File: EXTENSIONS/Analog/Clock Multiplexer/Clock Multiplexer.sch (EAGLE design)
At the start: 13 parts

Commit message: update clock multiplexer
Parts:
- removed SJ1: (no value), microbuilder:SOLDERJUMPERREFLOW
- added AUTOMATED_CLOCK_ON_OFF: (no value), adafruit:EG1218S
- renumbered R_MANUAL_CLOCK_PULL_DOWN to R_MANUAL_CLOCK_PULL_DOWN_1K
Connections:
- net N$2: now also AUTOMATED_CLOCK_ON_OFF.P; no longer SJ1.2
- net TMR555_OUTPUT_2: now also AUTOMATED_CLOCK_ON_OFF.O; no longer SJ1.1
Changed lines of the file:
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@@
 <part name="GND8" library="supply1" deviceset="GND" device=""/>
 <part name="MANUAL_CLOCK" library="switch-omron" deviceset="10-XX" device=""/>
-<part name="R_MANUAL_CLOCK_PULL_DOWN" library="adafruit" deviceset="R-US_" device="R1206"/>
+<part name="R_MANUAL_CLOCK_PULL_DOWN_1K" library="adafruit" deviceset="R-US_" device="R1206"/>
 <part name="GND9" library="supply1" deviceset="GND" device=""/>
-<part name="SJ1" library="microbuilder" deviceset="SOLDERJUMPER" device="REFLOW"/>
 <part name="DIODE_1N5817" library="diode" deviceset="1N821" device=""/>
+<part name="AUTOMATED_CLOCK_ON_OFF" library="adafruit" deviceset="EG1218" device="S"/>
 </parts>
 <sheets>
@@
 <instance part="GND8" gate="1" x="-66.04" y="81.28"/>
 <instance part="MANUAL_CLOCK" gate="1" x="-73.66" y="53.34"/>
-<instance part="R_MANUAL_CLOCK_PULL_DOWN" gate="G$1" x="-86.36" y="40.64"/>
+<instance part="R_MANUAL_CLOCK_PULL_DOWN_1K" gate="G$1" x="-86.36" y="40.64"/>
 <instance part="GND9" gate="1" x="-106.68" y="40.64" rot="R270"/>
-<instance part="SJ1" gate="1" x="-40.64" y="129.54"/>
 <instance part="DIODE_1N5817" gate="1" x="-25.4" y="129.54" rot="R180"/>
+<instance part="AUTOMATED_CLOCK_ON_OFF" gate="1" x="-48.26" y="127" smashed="yes" rot="R90">
+<attribute name="NAME" x="-43.053" y="136.652" size="1.778" layer="95" rot="R180"/>
+<attribute name="VALUE" x="-51.435" y="123.19" size="1.778" layer="96" rot="R180"/>
+</instance>
 </instances>
 <busses>
@@
 <segment>
 <pinref part="GND9" gate="1" pin="GND"/>
-<pinref part="R_MANUAL_CLOCK_PULL_DOWN" gate="G$1" pin="1"/>
+<pinref part="R_MANUAL_CLOCK_PULL_DOWN_1K" gate="G$1" pin="1"/>
 <wire x1="-104.14" y1="40.64" x2="-91.44" y2="40.64" width="0.1524" layer="91"/>
 </segment>
@@
 <wire x1="-71.12" y1="48.26" x2="-71.12" y2="40.64" width="0.1524" layer="91"/>
 <label x="-71.12" y="38.1" size="1.778" layer="95"/>
-<pinref part="R_MANUAL_CLOCK_PULL_DOWN" gate="G$1" pin="2"/>
+<pinref part="R_MANUAL_CLOCK_PULL_DOWN_1K" gate="G$1" pin="2"/>
 <wire x1="-71.12" y1="40.64" x2="-71.12" y2="35.56" width="0.1524" layer="91"/>
 <wire x1="-81.28" y1="40.64" x2="-71.12" y2="40.64" width="0.1524" layer="91"/>
@@
 </segment>
 <segment>
-<pinref part="SJ1" gate="1" pin="1"/>
-<wire x1="-45.72" y1="129.54" x2="-60.96" y2="129.54" width="0.1524" layer="91"/>
-<label x="-60.96" y="129.54" size="1.778" layer="95" rot="R180"/>
+<pinref part="AUTOMATED_CLOCK_ON_OFF" gate="1" pin="O"/>
+<wire x1="-53.34" y1="127" x2="-71.12" y2="127" width="0.1524" layer="91"/>
+<label x="-75.184" y="127.762" size="1.778" layer="95"/>
 </segment>
 </net>
@@
 <segment>
 <pinref part="DIODE_1N5817" gate="1" pin="C"/>
-<pinref part="SJ1" gate="1" pin="2"/>
-<wire x1="-27.94" y1="129.54" x2="-35.56" y2="129.54" width="0.1524" layer="91"/>
-</segment>
-</net>
+<pinref part="AUTOMATED_CLOCK_ON_OFF" gate="1" pin="P"/>
+<wire x1="-27.94" y1="129.54" x2="-43.18" y2="129.54" width="0.1524" layer="91"/>
+</segment>
+</net>

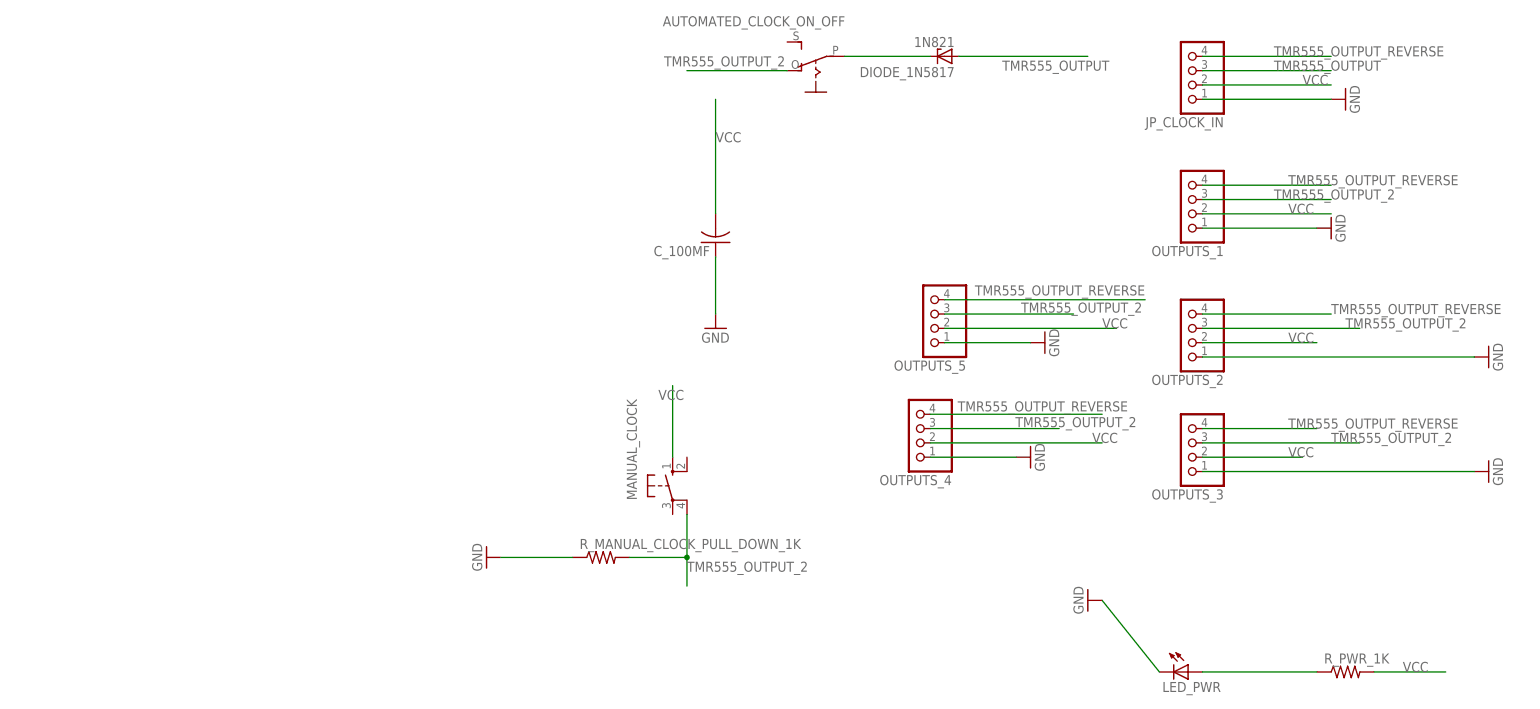
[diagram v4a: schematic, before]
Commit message: Create v2 of Clock de-multiplexer
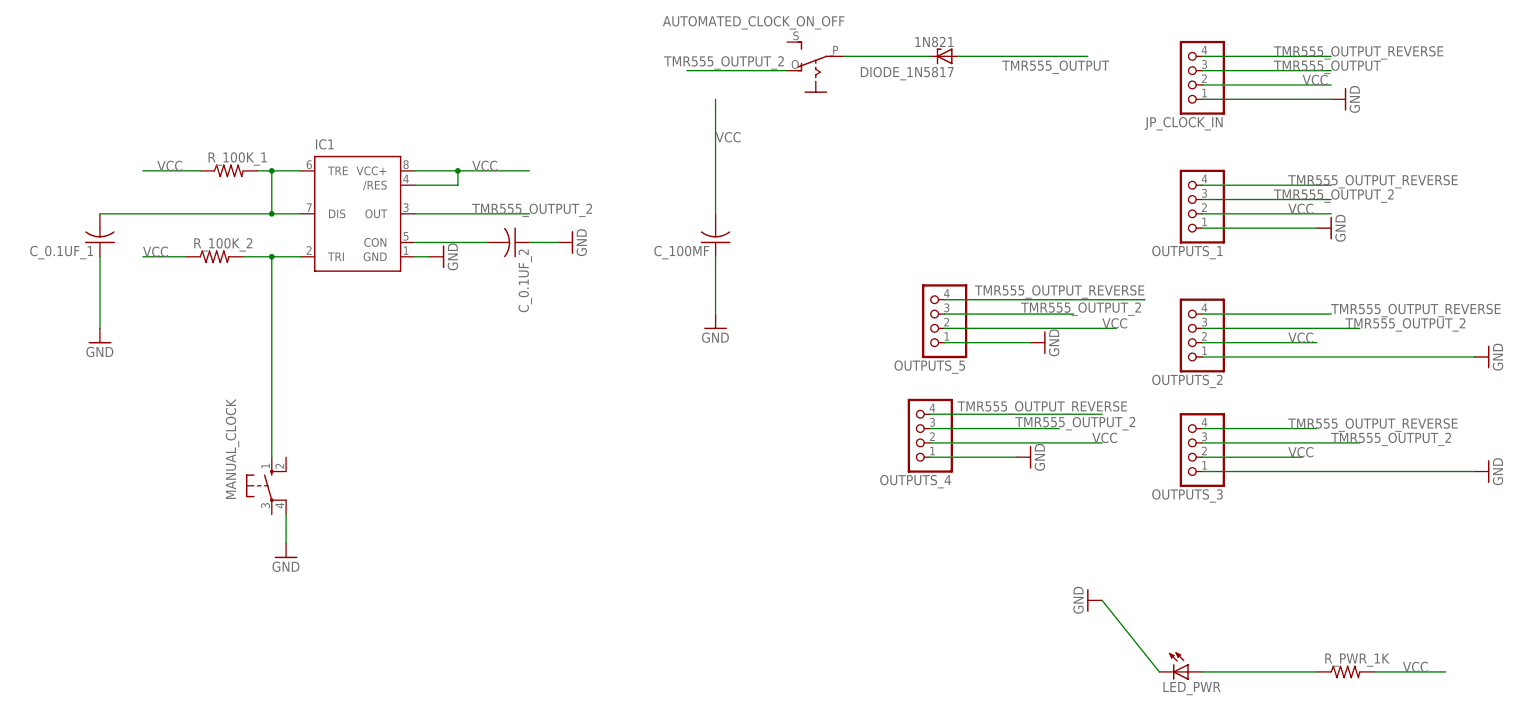
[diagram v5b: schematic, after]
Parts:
- removed R_MANUAL_CLOCK_PULL_DOWN_1K: (no value), adafruit:R-US_R1206
- added C_0.1UF_1, C_0.1UF_2: (no value), adafruit:C-USC1206
- added IC1: (no value), SparkFun-AnalogIC:NE555D
- added R_100K_1, R_100K_2: (no value), adafruit:R-US_R1206
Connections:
- new net N$3: C_0.1UF_1.2, IC1.DIS, IC1.TRE, R_100K_1.2
- new net N$4: C_0.1UF_2.2, IC1.CON
- new net N$5: IC1.TRI, MANUAL_CLOCK.S, R_100K_2.2
- net GND: now also C_0.1UF_1.1, C_0.1UF_2.1, IC1.GND, MANUAL_CLOCK.P1; no longer R_MANUAL_CLOCK_PULL_DOWN_1K.1
- net TMR555_OUTPUT_2: now also IC1.OUT; no longer MANUAL_CLOCK.P1, R_MANUAL_CLOCK_PULL_DOWN_1K.2
- net VCC: now also IC1./RES, IC1.VCC+, R_100K_1.1, R_100K_2.1; no longer MANUAL_CLOCK.S
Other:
- moved on the sheet: MANUAL_CLOCK
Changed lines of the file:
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@@
 <part name="GND8" library="supply1" deviceset="GND" device=""/>
 <part name="MANUAL_CLOCK" library="switch-omron" deviceset="10-XX" device=""/>
-<part name="R_MANUAL_CLOCK_PULL_DOWN_1K" library="adafruit" deviceset="R-US_" device="R1206"/>
-<part name="GND9" library="supply1" deviceset="GND" device=""/>
 <part name="DIODE_1N5817" library="diode" deviceset="1N821" device=""/>
 <part name="AUTOMATED_CLOCK_ON_OFF" library="adafruit" deviceset="EG1218" device="S"/>
+<part name="IC1" library="SparkFun-AnalogIC" deviceset="NE555" device="D"/>
+<part name="R_100K_1" library="adafruit" deviceset="R-US_" device="R1206"/>
+<part name="C_0.1UF_1" library="adafruit" deviceset="C-US" device="C1206"/>
+<part name="GND10" library="supply1" deviceset="GND" device=""/>
+<part name="GND11" library="supply1" deviceset="GND" device=""/>
+<part name="C_0.1UF_2" library="adafruit" deviceset="C-US" device="C1206"/>
+<part name="GND12" library="supply1" deviceset="GND" device=""/>
+<part name="R_100K_2" library="adafruit" deviceset="R-US_" device="R1206"/>
+<part name="GND9" library="supply1" deviceset="GND" device=""/>
 </parts>
 <sheets>
@@
 <instance part="C_100MF" gate="G$1" x="-66.04" y="96.52" rot="R180"/>
 <instance part="GND8" gate="1" x="-66.04" y="81.28"/>
-<instance part="MANUAL_CLOCK" gate="1" x="-73.66" y="53.34"/>
-<instance part="R_MANUAL_CLOCK_PULL_DOWN_1K" gate="G$1" x="-86.36" y="40.64"/>
-<instance part="GND9" gate="1" x="-106.68" y="40.64" rot="R270"/>
+<instance part="MANUAL_CLOCK" gate="1" x="-144.78" y="53.34"/>
 <instance part="DIODE_1N5817" gate="1" x="-25.4" y="129.54" rot="R180"/>
 <instance part="AUTOMATED_CLOCK_ON_OFF" gate="1" x="-48.26" y="127" smashed="yes" rot="R90">
@@
 <attribute name="VALUE" x="-51.435" y="123.19" size="1.778" layer="96" rot="R180"/>
 </instance>
+<instance part="IC1" gate="G$1" x="-129.54" y="101.6"/>
+<instance part="R_100K_1" gate="G$1" x="-152.4" y="109.22"/>
+<instance part="C_0.1UF_1" gate="G$1" x="-175.26" y="96.52" rot="R180"/>
+<instance part="GND10" gate="1" x="-175.26" y="78.74"/>
+<instance part="GND11" gate="1" x="-114.3" y="93.98" rot="R90"/>
+<instance part="C_0.1UF_2" gate="G$1" x="-101.6" y="96.52" rot="R270"/>
+<instance part="GND12" gate="1" x="-91.44" y="96.52" rot="R90"/>
+<instance part="R_100K_2" gate="G$1" x="-154.94" y="93.98"/>
+<instance part="GND9" gate="1" x="-142.24" y="40.64"/>
 </instances>
 <busses>
@@
 </segment>
 <segment>
+<pinref part="C_0.1UF_1" gate="G$1" pin="1"/>
+<pinref part="GND10" gate="1" pin="GND"/>
+<wire x1="-175.26" y1="93.98" x2="-175.26" y2="81.28" width="0.1524" layer="91"/>
+</segment>
+<segment>
+<pinref part="IC1" gate="G$1" pin="GND"/>
+<pinref part="GND11" gate="1" pin="GND"/>
+<wire x1="-119.38" y1="93.98" x2="-116.84" y2="93.98" width="0.1524" layer="91"/>
+</segment>
+<segment>
+<pinref part="GND12" gate="1" pin="GND"/>
+<pinref part="C_0.1UF_2" gate="G$1" pin="1"/>
+<wire x1="-93.98" y1="96.52" x2="-99.06" y2="96.52" width="0.1524" layer="91"/>
+</segment>
+<segment>
+<pinref part="MANUAL_CLOCK" gate="1" pin="P1"/>
 <pinref part="GND9" gate="1" pin="GND"/>
-<pinref part="R_MANUAL_CLOCK_PULL_DOWN_1K" gate="G$1" pin="1"/>
-<wire x1="-104.14" y1="40.64" x2="-91.44" y2="40.64" width="0.1524" layer="91"/>
+<wire x1="-142.24" y1="48.26" x2="-142.24" y2="43.18" width="0.1524" layer="91"/>
 </segment>
 </net>
@@
 </segment>
 <segment>
-<pinref part="MANUAL_CLOCK" gate="1" pin="S"/>
-<wire x1="-73.66" y1="58.42" x2="-73.66" y2="71.12" width="0.1524" layer="91"/>
-<label x="-76.2" y="68.58" size="1.778" layer="95"/>
+<pinref part="IC1" gate="G$1" pin="VCC+"/>
+<wire x1="-119.38" y1="109.22" x2="-111.76" y2="109.22" width="0.1524" layer="91"/>
+<label x="-109.22" y="109.22" size="1.778" layer="95"/>
+<pinref part="IC1" gate="G$1" pin="/RES"/>
+<wire x1="-111.76" y1="109.22" x2="-99.06" y2="109.22" width="0.1524" layer="91"/>
+<wire x1="-119.38" y1="106.68" x2="-111.76" y2="106.68" width="0.1524" layer="91"/>
+<wire x1="-111.76" y1="106.68" x2="-111.76" y2="109.22" width="0.1524" layer="91"/>
+<junction x="-111.76" y="109.22"/>
+</segment>
+<segment>
+<pinref part="R_100K_1" gate="G$1" pin="1"/>
+<wire x1="-157.48" y1="109.22" x2="-167.64" y2="109.22" width="0.1524" layer="91"/>
+<label x="-165.1" y="109.22" size="1.778" layer="95"/>
+</segment>
+<segment>
+<pinref part="R_100K_2" gate="G$1" pin="1"/>
+<wire x1="-160.02" y1="93.98" x2="-167.64" y2="93.98" width="0.1524" layer="91"/>
+<label x="-167.64" y="93.98" size="1.778" layer="95"/>
 </segment>
 </net>
@@
 </segment>
 <segment>
-<pinref part="MANUAL_CLOCK" gate="1" pin="P1"/>
-<wire x1="-71.12" y1="48.26" x2="-71.12" y2="40.64" width="0.1524" layer="91"/>
-<label x="-71.12" y="38.1" size="1.778" layer="95"/>
-<pinref part="R_MANUAL_CLOCK_PULL_DOWN_1K" gate="G$1" pin="2"/>
-<wire x1="-71.12" y1="40.64" x2="-71.12" y2="35.56" width="0.1524" layer="91"/>
-<wire x1="-81.28" y1="40.64" x2="-71.12" y2="40.64" width="0.1524" layer="91"/>
-<junction x="-71.12" y="40.64"/>
-</segment>
-<segment>
 <pinref part="AUTOMATED_CLOCK_ON_OFF" gate="1" pin="O"/>
 <wire x1="-53.34" y1="127" x2="-71.12" y2="127" width="0.1524" layer="91"/>
 <label x="-75.184" y="127.762" size="1.778" layer="95"/>
 </segment>
+<segment>
+<pinref part="IC1" gate="G$1" pin="OUT"/>
+<wire x1="-119.38" y1="101.6" x2="-99.06" y2="101.6" width="0.1524" layer="91"/>
+<label x="-109.22" y="101.6" size="1.778" layer="95"/>
+</segment>
 </net>
 <net name="N$2" class="0">
@@
 </segment>
 </net>
+<net name="N$3" class="0">
+<segment>
+<pinref part="R_100K_1" gate="G$1" pin="2"/>
+<pinref part="IC1" gate="G$1" pin="TRE"/>
+<wire x1="-147.32" y1="109.22" x2="-144.78" y2="109.22" width="0.1524" layer="91"/>
+<pinref part="IC1" gate="G$1" pin="DIS"/>
+<wire x1="-144.78" y1="109.22" x2="-139.7" y2="109.22" width="0.1524" layer="91"/>
+<wire x1="-139.7" y1="101.6" x2="-144.78" y2="101.6" width="0.1524" layer="91"/>
+<wire x1="-144.78" y1="101.6" x2="-144.78" y2="109.22" width="0.1524" layer="91"/>
+<junction x="-144.78" y="109.22"/>
+<pinref part="C_0.1UF_1" gate="G$1" pin="2"/>
+<wire x1="-144.78" y1="101.6" x2="-175.26" y2="101.6" width="0.1524" layer="91"/>
+<junction x="-144.78" y="101.6"/>
+</segment>
+</net>
+<net name="N$4" class="0">
+<segment>
+<pinref part="IC1" gate="G$1" pin="CON"/>
+<pinref part="C_0.1UF_2" gate="G$1" pin="2"/>
+<wire x1="-119.38" y1="96.52" x2="-106.68" y2="96.52" width="0.1524" layer="91"/>
+</segment>
+</net>
+<net name="N$5" class="0">
+<segment>
+<pinref part="R_100K_2" gate="G$1" pin="2"/>
+<pinref part="IC1" gate="G$1" pin="TRI"/>
+<wire x1="-149.86" y1="93.98" x2="-144.78" y2="93.98" width="0.1524" layer="91"/>
+<pinref part="MANUAL_CLOCK" gate="1" pin="S"/>
+<wire x1="-144.78" y1="93.98" x2="-139.7" y2="93.98" width="0.1524" layer="91"/>
+<wire x1="-144.78" y1="58.42" x2="-144.78" y2="93.98" width="0.1524" layer="91"/>
+<junction x="-144.78" y="93.98"/>
+</segment>
+</net>

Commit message: Create v2 of Clock de-multiplexer
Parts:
- renumbered C_100MF to C_100UF, IC1 to TIMER_555
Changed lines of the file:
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@@
 <part name="GND6" library="supply1" deviceset="GND" device=""/>
 <part name="GND7" library="supply1" deviceset="GND" device=""/>
-<part name="C_100MF" library="adafruit" deviceset="C-US" device="025-030X050"/>
+<part name="C_100UF" library="adafruit" deviceset="C-US" device="025-030X050"/>
 <part name="GND8" library="supply1" deviceset="GND" device=""/>
 <part name="MANUAL_CLOCK" library="switch-omron" deviceset="10-XX" device=""/>
 <part name="DIODE_1N5817" library="diode" deviceset="1N821" device=""/>
 <part name="AUTOMATED_CLOCK_ON_OFF" library="adafruit" deviceset="EG1218" device="S"/>
-<part name="IC1" library="SparkFun-AnalogIC" deviceset="NE555" device="D"/>
+<part name="TIMER_555" library="SparkFun-AnalogIC" deviceset="NE555" device="D"/>
 <part name="R_100K_1" library="adafruit" deviceset="R-US_" device="R1206"/>
 <part name="C_0.1UF_1" library="adafruit" deviceset="C-US" device="C1206"/>
@@
 <instance part="GND6" gate="1" x="-7.62" y="78.74" rot="R90"/>
 <instance part="GND7" gate="1" x="-10.16" y="58.42" rot="R90"/>
-<instance part="C_100MF" gate="G$1" x="-66.04" y="96.52" rot="R180"/>
+<instance part="C_100UF" gate="G$1" x="-66.04" y="96.52" rot="R180"/>
 <instance part="GND8" gate="1" x="-66.04" y="81.28"/>
 <instance part="MANUAL_CLOCK" gate="1" x="-144.78" y="53.34"/>
@@
 <attribute name="VALUE" x="-51.435" y="123.19" size="1.778" layer="96" rot="R180"/>
 </instance>
-<instance part="IC1" gate="G$1" x="-129.54" y="101.6"/>
+<instance part="TIMER_555" gate="G$1" x="-129.54" y="101.6"/>
 <instance part="R_100K_1" gate="G$1" x="-152.4" y="109.22"/>
 <instance part="C_0.1UF_1" gate="G$1" x="-175.26" y="96.52" rot="R180"/>
@@
 </segment>
 <segment>
-<pinref part="C_100MF" gate="G$1" pin="1"/>
+<pinref part="C_100UF" gate="G$1" pin="1"/>
 <pinref part="GND8" gate="1" pin="GND"/>
 <wire x1="-66.04" y1="93.98" x2="-66.04" y2="83.82" width="0.1524" layer="91"/>
@@
 </segment>
 <segment>
-<pinref part="IC1" gate="G$1" pin="GND"/>
+<pinref part="TIMER_555" gate="G$1" pin="GND"/>
 <pinref part="GND11" gate="1" pin="GND"/>
 <wire x1="-119.38" y1="93.98" x2="-116.84" y2="93.98" width="0.1524" layer="91"/>
@@
 </segment>
 <segment>
-<pinref part="C_100MF" gate="G$1" pin="2"/>
+<pinref part="C_100UF" gate="G$1" pin="2"/>
 <wire x1="-66.04" y1="101.6" x2="-66.04" y2="121.92" width="0.1524" layer="91"/>
 <label x="-66.04" y="114.3" size="1.778" layer="95"/>
 </segment>
 <segment>
-<pinref part="IC1" gate="G$1" pin="VCC+"/>
+<pinref part="TIMER_555" gate="G$1" pin="VCC+"/>
 <wire x1="-119.38" y1="109.22" x2="-111.76" y2="109.22" width="0.1524" layer="91"/>
 <label x="-109.22" y="109.22" size="1.778" layer="95"/>
-<pinref part="IC1" gate="G$1" pin="/RES"/>
+<pinref part="TIMER_555" gate="G$1" pin="/RES"/>
 <wire x1="-111.76" y1="109.22" x2="-99.06" y2="109.22" width="0.1524" layer="91"/>
 <wire x1="-119.38" y1="106.68" x2="-111.76" y2="106.68" width="0.1524" layer="91"/>
@@
 </segment>
 <segment>
-<pinref part="IC1" gate="G$1" pin="OUT"/>
+<pinref part="TIMER_555" gate="G$1" pin="OUT"/>
 <wire x1="-119.38" y1="101.6" x2="-99.06" y2="101.6" width="0.1524" layer="91"/>
 <label x="-109.22" y="101.6" size="1.778" layer="95"/>
@@
 <segment>
 <pinref part="R_100K_1" gate="G$1" pin="2"/>
-<pinref part="IC1" gate="G$1" pin="TRE"/>
+<pinref part="TIMER_555" gate="G$1" pin="TRE"/>
 <wire x1="-147.32" y1="109.22" x2="-144.78" y2="109.22" width="0.1524" layer="91"/>
-<pinref part="IC1" gate="G$1" pin="DIS"/>
+<pinref part="TIMER_555" gate="G$1" pin="DIS"/>
 <wire x1="-144.78" y1="109.22" x2="-139.7" y2="109.22" width="0.1524" layer="91"/>
 <wire x1="-139.7" y1="101.6" x2="-144.78" y2="101.6" width="0.1524" layer="91"/>
@@
 <net name="N$4" class="0">
 <segment>
-<pinref part="IC1" gate="G$1" pin="CON"/>
+<pinref part="TIMER_555" gate="G$1" pin="CON"/>
 <pinref part="C_0.1UF_2" gate="G$1" pin="2"/>
 <wire x1="-119.38" y1="96.52" x2="-106.68" y2="96.52" width="0.1524" layer="91"/>
@@
 <segment>
 <pinref part="R_100K_2" gate="G$1" pin="2"/>
-<pinref part="IC1" gate="G$1" pin="TRI"/>
+<pinref part="TIMER_555" gate="G$1" pin="TRI"/>
 <wire x1="-149.86" y1="93.98" x2="-144.78" y2="93.98" width="0.1524" layer="91"/>
 <pinref part="MANUAL_CLOCK" gate="1" pin="S"/>
